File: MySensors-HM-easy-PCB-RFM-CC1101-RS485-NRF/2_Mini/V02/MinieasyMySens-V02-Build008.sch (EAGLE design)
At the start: 24 parts, among them IC1 ATSHA204A, IC2 REG1117, M1 ARDUINO-PRO-MINI-3.3V#NP

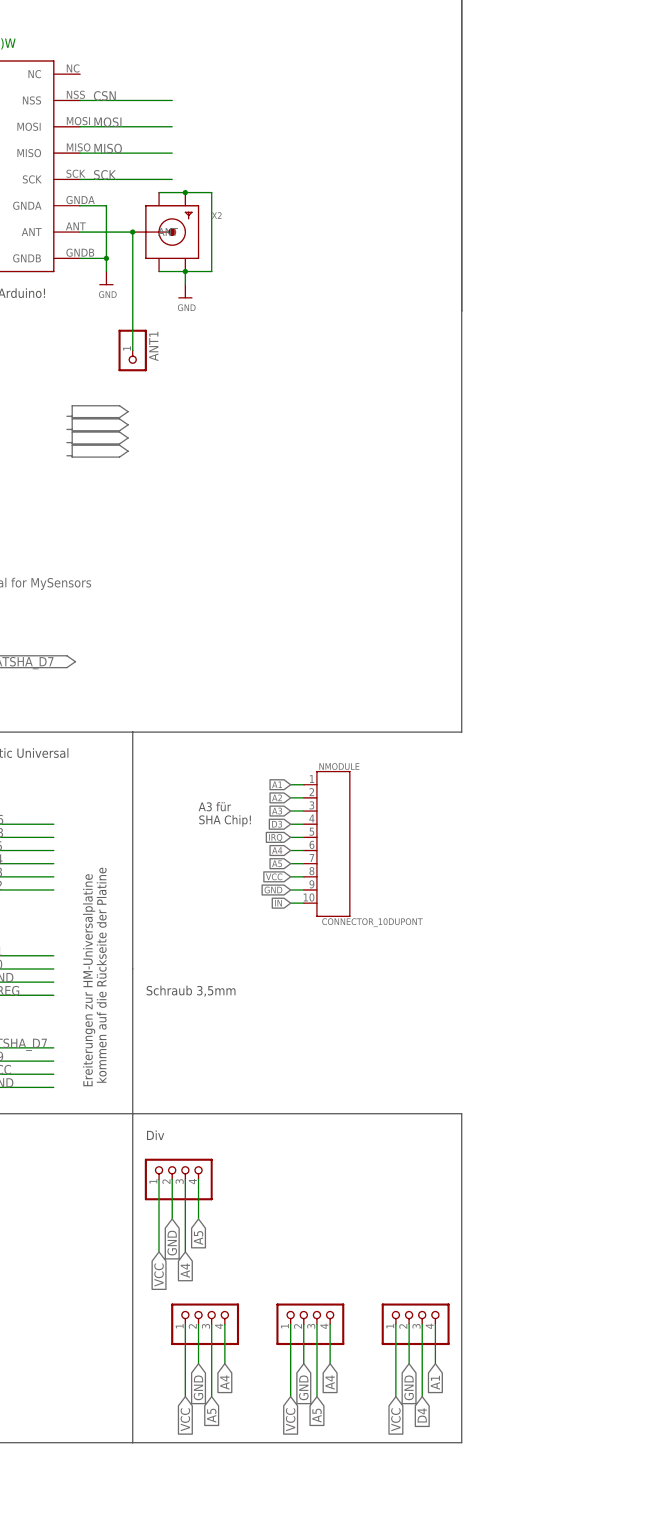
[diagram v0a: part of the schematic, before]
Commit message: Update RFM95
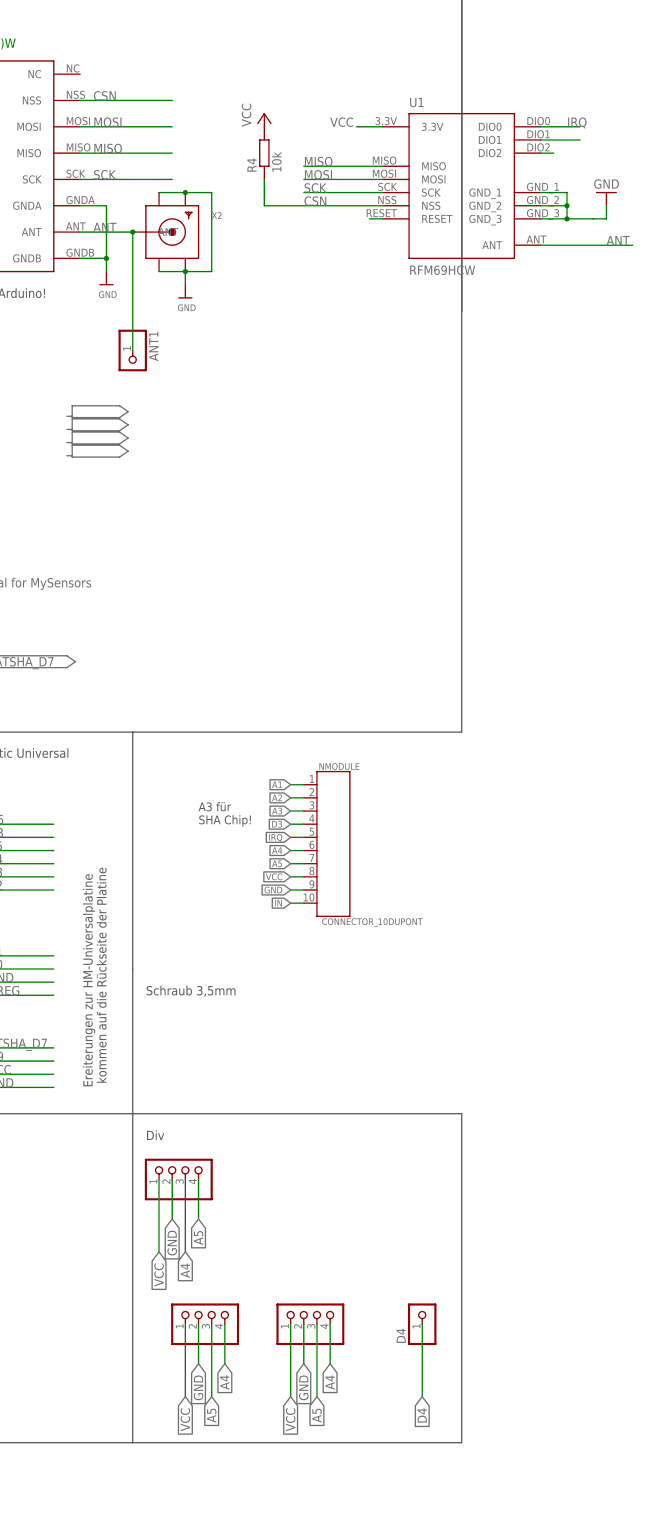
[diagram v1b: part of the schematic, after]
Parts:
- removed MOTION: (no value), pinhead-2:PINHD-1X04_2.54-S
- added D4: (no value), pinhead:PINHD-1X1
- added R4: 10k, rcl:R-EU_M0805
- added U1: RFM69HCW, doug:RFM69HCW
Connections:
- removed net N$16: ANT1.1, RFM69W.ANT, X2.ANT
- new net ANT: ANT1.1, RFM69W.ANT, U1.ANT, X2.ANT
- new net N$1: U1.RESET
- new net N$14: U1.DIO2
- new net N$15: U1.DIO1
- net A1: no longer MOTION.4
- net CSN: now also R4.1, U1.NSS
- net D4: now also D4.1; no longer MOTION.3
- net GND: now also U1.GND_1, U1.GND_2, U1.GND_3; no longer MOTION.2
- net IRQ: now also U1.DIO0
- net MISO: now also U1.MISO
- net MOSI: now also U1.MOSI
- net SCK: now also U1.SCK
- net VCC: now also R4.2, U1.3.3V; no longer MOTION.1
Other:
- note removed: "Motion"
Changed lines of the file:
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@@
 <layers>
 <layer number="1" name="Top" color="4" fill="1" visible="no" active="no"/>
+<layer number="2" name="Route2" color="1" fill="3" visible="no" active="no"/>
+<layer number="3" name="Route3" color="4" fill="3" visible="no" active="no"/>
+<layer number="4" name="Route4" color="1" fill="4" visible="no" active="no"/>
+<layer number="5" name="Route5" color="4" fill="4" visible="no" active="no"/>
+<layer number="6" name="Route6" color="1" fill="8" visible="no" active="no"/>
+<layer number="7" name="Route7" color="4" fill="8" visible="no" active="no"/>
+<layer number="8" name="Route8" color="1" fill="2" visible="no" active="no"/>
+<layer number="9" name="Route9" color="4" fill="2" visible="no" active="no"/>
+<layer number="10" name="Route10" color="1" fill="7" visible="no" active="no"/>
+<layer number="11" name="Route11" color="4" fill="7" visible="no" active="no"/>
+<layer number="12" name="Route12" color="1" fill="5" visible="no" active="no"/>
+<layer number="13" name="Route13" color="4" fill="5" visible="no" active="no"/>
+<layer number="14" name="Route14" color="1" fill="6" visible="no" active="no"/>
+<layer number="15" name="Route15" color="4" fill="6" visible="no" active="no"/>
 <layer number="16" name="Bottom" color="1" fill="1" visible="no" active="no"/>
 <layer number="17" name="Pads" color="2" fill="1" visible="no" active="no"/>
@@
 <part name="I2C-1" library="pinhead-2" deviceset="PINHD-1X04" device="_2.54-S"/>
 <part name="I2C-2" library="pinhead-2" deviceset="PINHD-1X04" device="_2.54-S"/>
-<part name="MOTION" library="pinhead-2" deviceset="PINHD-1X04" device="_2.54-S"/>
 <part name="HM2" library="SparkFun-Connectors" deviceset="CONN_06" device="SILK_FEMALE_PTH"/>
 <part name="HM1" library="SparkFun-Connectors" deviceset="CONN_04" device=""/>
@@
 <part name="R7" library="rcl" deviceset="R-EU_" device="R0805" value="10K"/>
 <part name="JP19" library="pinhead" deviceset="PINHD-1X2" device=""/>
+<part name="GND21" library="doug" deviceset="GND" device=""/>
+<part name="R4" library="rcl" deviceset="R-EU_" device="M0805" value="10k"/>
+<part name="P+6" library="doug" deviceset="VCC" device=""/>
+<part name="U1" library="doug" deviceset="RFM69H" device="CW"/>
+<part name="D4" library="pinhead" deviceset="PINHD-1X1" device=""/>
 </parts>
 <sheets>
@@
 von GND.3 der A5 Pin ist verbinden !!! </text>
 <text x="111.76" y="-35.56" size="1.778" layer="104">BMP280</text>
-<text x="132.08" y="-35.56" size="1.778" layer="104">Motion</text>
 <text x="58.42" y="10.16" size="1.27" layer="102">??? B1 ??</text>
 <text x="93.98" y="55.88" size="1.6764" layer="97">A3 für
@@
 <attribute name="VALUE" x="99.06" y="-16.51" size="1.778" layer="96" rot="R90"/>
 </instance>
-<instance part="MOTION" gate="A" x="137.16" y="-38.1" smashed="yes" rot="R90">
-<attribute name="VALUE" x="144.78" y="-44.45" size="1.778" layer="96" rot="R90"/>
-</instance>
 <instance part="HM2" gate="G$1" x="48.26" y="48.26"/>
 <instance part="HM1" gate="G$1" x="48.26" y="25.4"/>
@@
 <instance part="R7" gate="G$1" x="-55.88" y="152.4" rot="R90"/>
 <instance part="JP19" gate="G$1" x="-86.36" y="22.86" rot="R90"/>
+<instance part="GND21" gate="1" x="172.72" y="177.8" rot="R180"/>
+<instance part="R4" gate="G$1" x="106.68" y="185.42" rot="R90"/>
+<instance part="P+6" gate="VCC" x="106.68" y="193.04"/>
+<instance part="U1" gate="G$1" x="144.78" y="177.8"/>
+<instance part="D4" gate="G$1" x="137.16" y="-38.1" rot="R90"/>
 </instances>
 <busses>
@@
 <label x="111.76" y="53.34" size="1.27" layer="95" rot="R180" xref="yes"/>
 </segment>
+<segment>
+<wire x1="160.02" y1="190.5" x2="167.64" y2="190.5" width="0.1524" layer="91"/>
+<label x="165.1" y="190.5" size="1.778" layer="95"/>
+<pinref part="U1" gate="G$1" pin="DIO0"/>
+</segment>
 </net>
 <net name="MISO" class="0">
@@
 <label x="73.66" y="185.42" size="1.778" layer="95"/>
 </segment>
+<segment>
+<wire x1="114.3" y1="182.88" x2="129.54" y2="182.88" width="0.1524" layer="91"/>
+<label x="114.3" y="182.88" size="1.778" layer="95"/>
+<pinref part="U1" gate="G$1" pin="MISO"/>
+</segment>
 </net>
 <net name="MOSI" class="0">
@@
 <label x="73.66" y="190.5" size="1.778" layer="95"/>
 </segment>
+<segment>
+<wire x1="129.54" y1="180.34" x2="114.3" y2="180.34" width="0.1524" layer="91"/>
+<label x="114.3" y="180.34" size="1.778" layer="95"/>
+<pinref part="U1" gate="G$1" pin="MOSI"/>
+</segment>
 </net>
 <net name="SCK" class="0">
@@
 <label x="73.66" y="180.34" size="1.778" layer="95"/>
 </segment>
+<segment>
+<wire x1="114.3" y1="177.8" x2="129.54" y2="177.8" width="0.1524" layer="91"/>
+<label x="114.3" y="177.8" size="1.778" layer="95"/>
+<pinref part="U1" gate="G$1" pin="SCK"/>
+</segment>
 </net>
 <net name="CSN" class="0">
@@
 <wire x1="71.12" y1="195.58" x2="88.9" y2="195.58" width="0.1524" layer="91"/>
 <label x="73.66" y="195.58" size="1.778" layer="95"/>
+</segment>
+<segment>
+<label x="114.3" y="175.26" size="1.778" layer="95"/>
+<pinref part="R4" gate="G$1" pin="1"/>
+<wire x1="129.54" y1="175.26" x2="106.68" y2="175.26" width="0.1524" layer="91"/>
+<wire x1="106.68" y1="175.26" x2="106.68" y2="180.34" width="0.1524" layer="91"/>
+<pinref part="U1" gate="G$1" pin="NSS"/>
 </segment>
 </net>
@@
 </segment>
 <segment>
-<pinref part="MOTION" gate="A" pin="2"/>
-<wire x1="134.62" y1="-40.64" x2="134.62" y2="-48.26" width="0.1524" layer="91"/>
-<label x="134.62" y="-48.26" size="1.778" layer="95" rot="R270" xref="yes"/>
-</segment>
-<segment>
 <pinref part="HM1" gate="G$1" pin="2"/>
 <wire x1="53.34" y1="25.4" x2="66.04" y2="25.4" width="0.1524" layer="91"/>
@@
 <wire x1="-88.9" y1="20.32" x2="-88.9" y2="12.7" width="0.1524" layer="91"/>
 <label x="-93.98" y="12.7" size="1.778" layer="95"/>
+</segment>
+<segment>
+<pinref part="GND21" gate="1" pin="GND"/>
+<wire x1="172.72" y1="172.72" x2="170.18" y2="172.72" width="0.1524" layer="91"/>
+<wire x1="170.18" y1="172.72" x2="165.1" y2="172.72" width="0.1524" layer="91"/>
+<wire x1="165.1" y1="172.72" x2="160.02" y2="172.72" width="0.1524" layer="91"/>
+<wire x1="172.72" y1="172.72" x2="172.72" y2="175.26" width="0.1524" layer="91"/>
+<pinref part="U1" gate="G$1" pin="GND_2"/>
+<wire x1="160.02" y1="175.26" x2="165.1" y2="175.26" width="0.1524" layer="91"/>
+<wire x1="165.1" y1="175.26" x2="165.1" y2="172.72" width="0.1524" layer="91"/>
+<junction x="165.1" y="172.72"/>
+<pinref part="U1" gate="G$1" pin="GND_1"/>
+<wire x1="160.02" y1="177.8" x2="165.1" y2="177.8" width="0.1524" layer="91"/>
+<wire x1="165.1" y1="177.8" x2="165.1" y2="175.26" width="0.1524" layer="91"/>
+<junction x="165.1" y="175.26"/>
+<pinref part="U1" gate="G$1" pin="GND_3"/>
 </segment>
 </net>
@@
 </segment>
 <segment>
-<pinref part="MOTION" gate="A" pin="1"/>
-<wire x1="132.08" y1="-40.64" x2="132.08" y2="-54.61" width="0.1524" layer="91"/>
-<label x="132.08" y="-54.61" size="1.778" layer="95" rot="R270" xref="yes"/>
-</segment>
-<segment>
 <pinref part="HM3" gate="G$1" pin="2"/>
 <wire x1="53.34" y1="7.62" x2="66.04" y2="7.62" width="0.1524" layer="91"/>
@@
 <wire x1="50.8" y1="91.44" x2="50.8" y2="96.52" width="0.1524" layer="91"/>
 <label x="50.8" y="96.52" size="1.778" layer="95"/>
+</segment>
+<segment>
+<pinref part="R4" gate="G$1" pin="2"/>
+<pinref part="P+6" gate="VCC" pin="VCC"/>
+</segment>
+<segment>
+<wire x1="129.54" y1="190.5" x2="124.46" y2="190.5" width="0.1524" layer="91"/>
+<label x="119.38" y="190.5" size="1.778" layer="95"/>
+<pinref part="U1" gate="G$1" pin="3.3V"/>
 </segment>
 </net>
@@
 </segment>
 <segment>
-<pinref part="MOTION" gate="A" pin="3"/>
 <wire x1="137.16" y1="-40.64" x2="137.16" y2="-54.61" width="0.1524" layer="91"/>
 <label x="137.16" y="-54.61" size="1.778" layer="95" rot="R270" xref="yes"/>
+<pinref part="D4" gate="G$1" pin="1"/>
 </segment>
 </net>
@@
 <label x="111.76" y="63.5" size="1.27" layer="95" rot="R180" xref="yes"/>
 </segment>
-<segment>
-<pinref part="MOTION" gate="A" pin="4"/>
-<wire x1="139.7" y1="-40.64" x2="139.7" y2="-48.26" width="0.1524" layer="91"/>
-<label x="139.7" y="-48.26" size="1.778" layer="95" rot="R270" xref="yes"/>
-</segment>
 </net>
 <net name="D6" class="0">
@@
 <wire x1="53.34" y1="12.7" x2="66.04" y2="12.7" width="0.1524" layer="91"/>
 <label x="53.34" y="12.7" size="1.778" layer="95"/>
-</segment>
-</net>
-<net name="N$16" class="0">
-<segment>
-<pinref part="RFM69W" gate="A" pin="ANT"/>
-<wire x1="71.12" y1="170.18" x2="81.28" y2="170.18" width="0.1524" layer="91"/>
-<pinref part="X2" gate="G$1" pin="ANT"/>
-<pinref part="ANT1" gate="G$1" pin="1"/>
-<wire x1="81.28" y1="170.18" x2="81.28" y2="147.32" width="0.1524" layer="91"/>
-<junction x="81.28" y="170.18"/>
 </segment>
 </net>
@@
 </segment>
 </net>
+<net name="ANT" class="0">
+<segment>
+<pinref part="U1" gate="G$1" pin="ANT"/>
+<wire x1="177.8" y1="167.64" x2="160.02" y2="167.64" width="0.1524" layer="91"/>
+<label x="172.72" y="167.64" size="1.778" layer="95"/>
+</segment>
+<segment>
+<pinref part="RFM69W" gate="A" pin="ANT"/>
+<wire x1="71.12" y1="170.18" x2="81.28" y2="170.18" width="0.1524" layer="91"/>
+<pinref part="X2" gate="G$1" pin="ANT"/>
+<pinref part="ANT1" gate="G$1" pin="1"/>
+<wire x1="81.28" y1="170.18" x2="81.28" y2="147.32" width="0.1524" layer="91"/>
+<junction x="81.28" y="170.18"/>
+<label x="73.66" y="170.18" size="1.778" layer="95"/>
+</segment>
+</net>
+<net name="N$14" class="0">
+<segment>
+<pinref part="U1" gate="G$1" pin="DIO2"/>
+<wire x1="160.02" y1="185.42" x2="162.56" y2="185.42" width="0.1524" layer="91"/>
+</segment>
+</net>
+<net name="N$15" class="0">
+<segment>
+<pinref part="U1" gate="G$1" pin="DIO1"/>
+<wire x1="160.02" y1="187.96" x2="167.64" y2="187.96" width="0.1524" layer="91"/>
+</segment>
+</net>
+<net name="N$1" class="0">
+<segment>
+<pinref part="U1" gate="G$1" pin="RESET"/>
+<wire x1="129.54" y1="172.72" x2="127" y2="172.72" width="0.1524" layer="91"/>
+</segment>
+</net>
